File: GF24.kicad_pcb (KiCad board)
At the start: 2 copper layers, 66 parts, among them J1 3220-10-0300-00, J2 2137160001, Q1 3904, Q2 DMN3731U-7, Q3 DMN3731U-7, Q4 DMP2004K-7, Q5 DMP2004K-7, Q6 DMP2004K-7, SW1 NRST, SW2 BOOT, SW3 ACTION, SW4 ON/OFF, SW5 MODE, U1 STM32F031C4T6, U2 SAM-M10Q, U3 TPS745, U4 LTC1733, U5 M24256, Y1 CS06465-32M

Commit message: some layout changes
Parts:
- removed J2: 2137160001, MB-Conn:MOLEX_2137160001
- added U6: 2137160001, MB-Conn:MOLEX_2137160001, F.Cu at (200.0, 87.0)
- BAT1: renamed from BAT+1; moved to B.Cu
- BAT2: renamed from BAT-1; moved to B.Cu
- C11, C12, C13, Q2, Q3, Q4, Q5, Q6, R10, R15, R16, R17, R18, R19, R20, R21, R22, R23, R5, R6, R7, R8, R9, TH1, U4: moved to B.Cu
- moved BAT1 120.3 mm to (169.8, 100.0), turned to 90 degrees
- moved U5 119.9 mm to (107.0, 151.0), turned to 90 degrees
- moved R11 106.6 mm to (103.8, 148.0)
- moved C14 106.0 mm to (103.5, 151.0), turned to -90 degrees
- moved C7 105.9 mm to (85.0, 92.0), turned to 90 degrees
- moved R12 102.9 mm to (107.0, 148.0)
- moved SW1 102.5 mm to (98.0, 130.0), turned to 90 degrees
- moved Q1 95.8 mm to (154.6, 131.1), turned to 180 degrees
- moved R1 95.6 mm to (108.8, 130.7), turned to -90 degrees
- moved C3 95.5 mm to (101.8, 141.0), turned to 90 degrees
- moved SW2 95.2 mm to (109.0, 125.8), turned to 180 degrees
- moved C1 94.2 mm to (111.8, 145.8), turned to 180 degrees
- moved C6 93.8 mm to (98.0, 141.0)
- moved C5 92.1 mm to (97.5, 136.5), turned to 180 degrees
- moved SW5 91.5 mm to (182.0, 86.8), turned to 180 degrees
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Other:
- board outline added: 125 x 40 mm

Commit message: 'test'
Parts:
- moved Q5 1.69 mm to (143.5, 60.6)

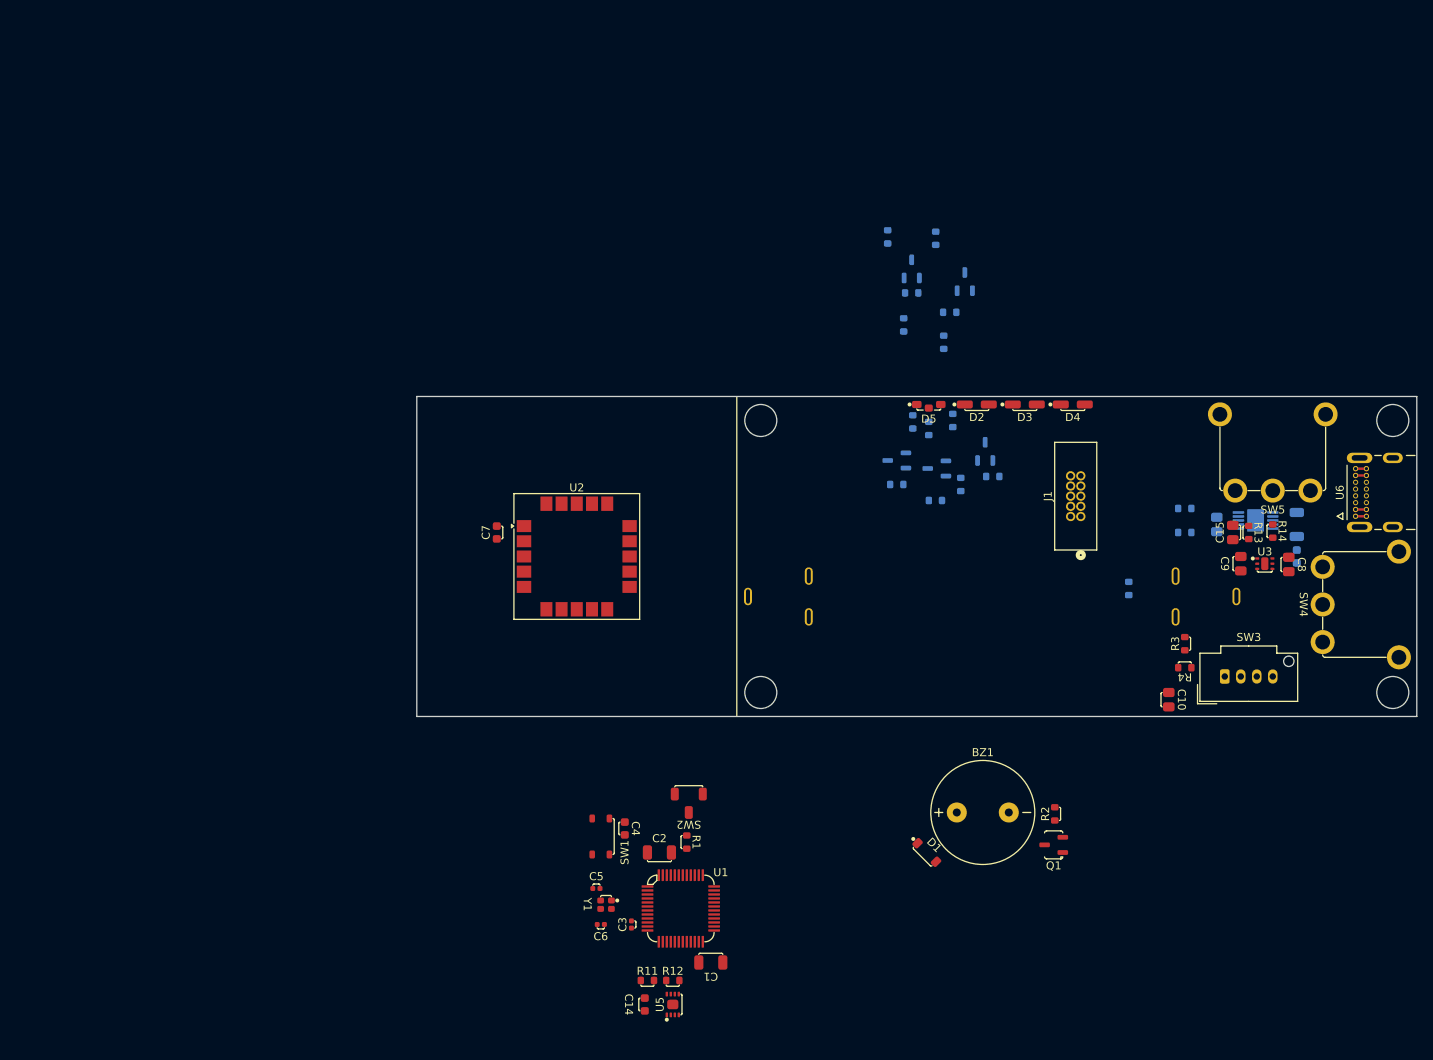
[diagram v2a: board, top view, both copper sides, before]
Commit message: started traces. need to check footprints are correct i.e. regulator
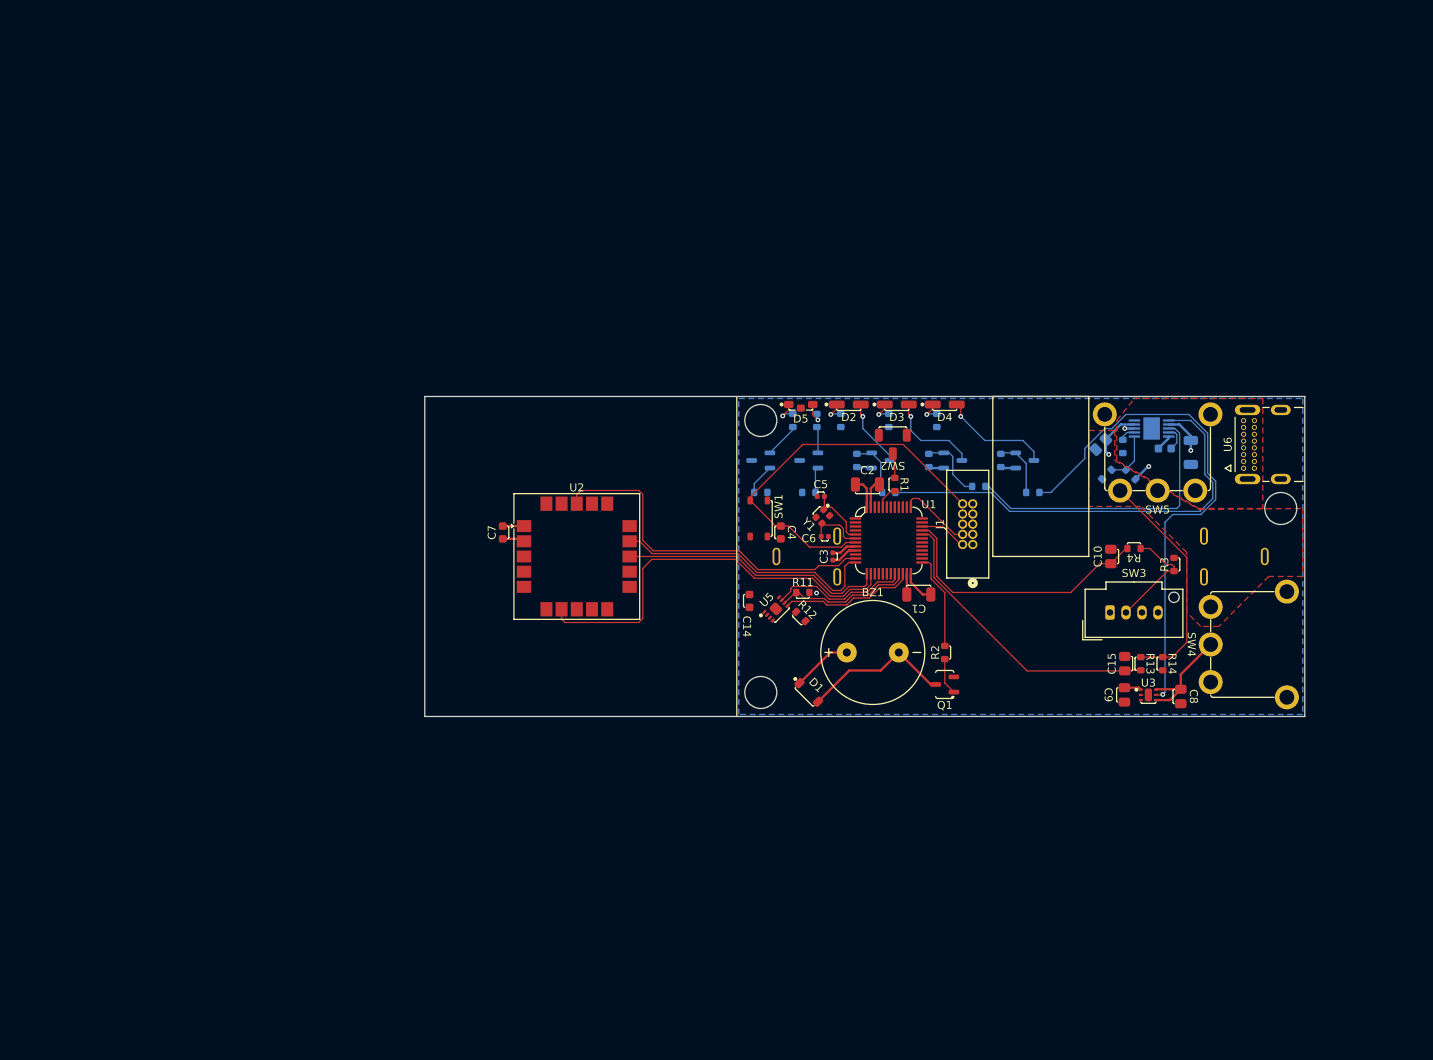
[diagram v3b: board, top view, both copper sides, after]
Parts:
- moved C5 56.5 mm to (125.5, 87.5)
- moved C6 56.0 mm to (126.0, 92.5)
- moved Y1 55.6 mm to (125.8, 90.0), turned to -135 degrees
- moved C2 52.8 mm to (131.3, 86.0)
- moved C1 52.8 mm to (137.8, 99.8)
- moved U1 52.8 mm to (134.0, 93.0)
- moved C3 52.4 mm to (127.0, 95.0)
- moved R11 52.2 mm to (123.2, 99.5)
- moved C14 52.1 mm to (116.6, 100.6)
- moved R1 51.7 mm to (134.8, 86.0)
- moved SW2 51.6 mm to (134.5, 81.0)
- moved U5 51.1 mm to (119.9, 101.6), turned to 45 degrees
- moved R12 48.2 mm to (123.0, 102.5), turned to -45 degrees
- moved SW1 44.4 mm to (117.8, 90.2)
- moved C4 41.8 mm to (120.5, 92.0)
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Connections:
- net +3V3 renamed 3V3
- net BAT- renamed GND
- net Net-(BZ1--) renamed /BUZZ-
- net Net-(D2-A) renamed /CHRG_QO
- net Net-(D2-K) renamed /CHRG_RES
- net Net-(D3-A) renamed /FAULT_QO
- net Net-(D3-K) renamed /FAULT_RES
- net Net-(D4-A) renamed /PG_QO
- net Net-(D4-K) renamed /PG_RES
- net Net-(D5-G) renamed /STATG_RES
- net Net-(D5-R) renamed /STATR_RES
- net Net-(Q1-B) renamed /BUZZ-QB
- net Net-(Q2-D) renamed /STATG_QI
- net Net-(Q2-G) renamed /STATG_QG
- net Net-(Q3-D) renamed /STATR_QI
- net Net-(Q3-G) renamed /STATR_QG
- net Net-(Q4-G) renamed /PG_QG
- net Net-(Q5-G) renamed /FAULT_QG
- net Net-(Q6-G) renamed /CHRG_QG
- net Net-(R3-Pad1) renamed /ACT-H
- net Net-(SW2-B) renamed /BOOT0_RES
- net Net-(SW4-B) renamed /REG_I
- net Net-(SW5-A) renamed /MODE-H
- net Net-(U4-NTC) renamed /CH-TH-DIV
- net Net-(U4-PROG) renamed /CH-PROG
- net Net-(U4-TIMER) renamed /CH-TIMER
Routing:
- net PG: track 0.00 -> 65.5 mm, vias 0 -> 1
- net N-CHRG: track 0.00 -> 55.0 mm
- net GNSS-TIMEPULSE: track 0.00 -> 50.9 mm
- net NRST: track 0.00 -> 48.6 mm
- net GNSS-N-RESET: track 0.00 -> 44.2 mm
- net MODE: track 0.00 -> 37.2 mm
- net N-FAULT: track 0.00 -> 36.2 mm
- net BUTTON: track 0.00 -> 33.9 mm
- net STM32-TX: track 0.00 -> 33.7 mm
- net STM32-RX: track 0.00 -> 33.4 mm
- net /MODE-H: track 0.00 -> 28.9 mm
- net 3V3: track 0.00 -> 25.8 mm
- net /BUZZ-: track 0.00 -> 18.9 mm
- net EEPROM-N-WC: track 0.00 -> 17.4 mm
- net SCL: track 0.00 -> 17.2 mm
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- added copper zone on F.Cu, net BAT+
- added copper zone on B.Cu, net GND
- added copper zone on F.Cu, net VBUS
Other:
- board size 125 x 40 mm -> 110 x 40 mm

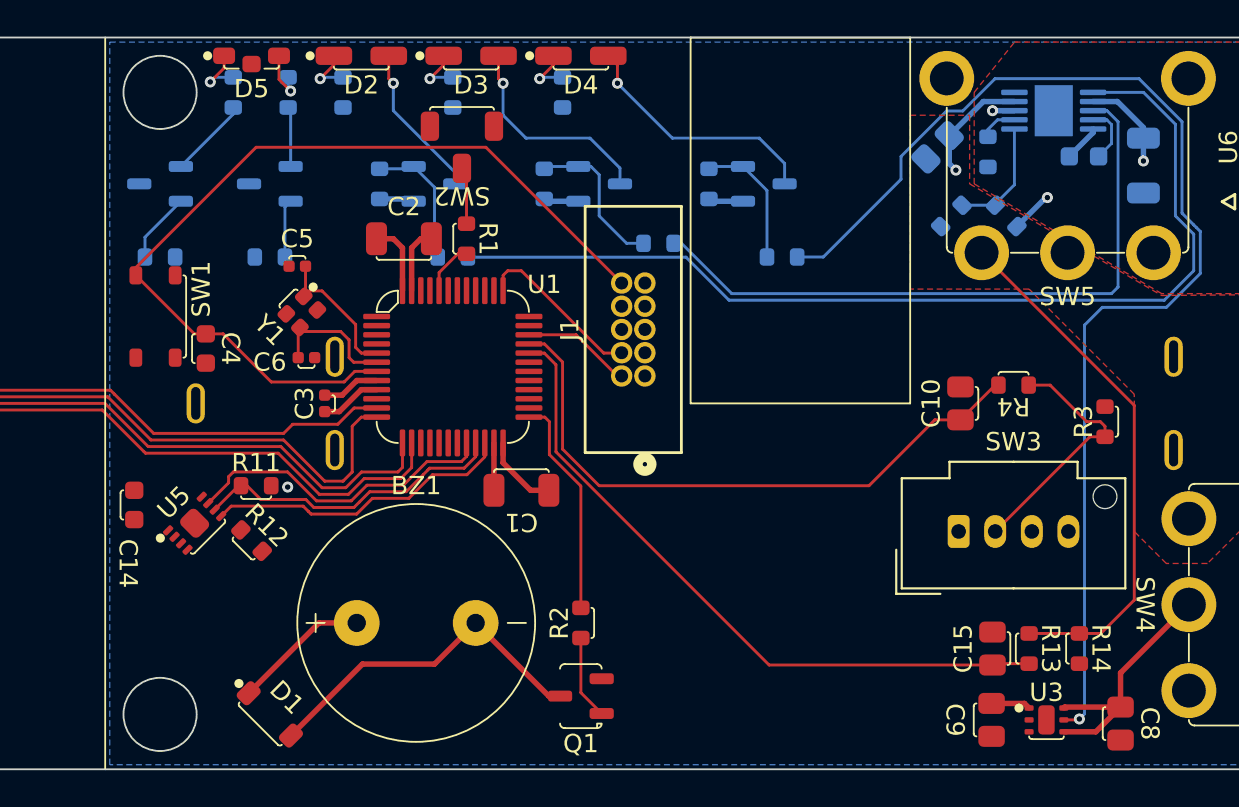
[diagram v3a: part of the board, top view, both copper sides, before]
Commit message: drew 3v plane
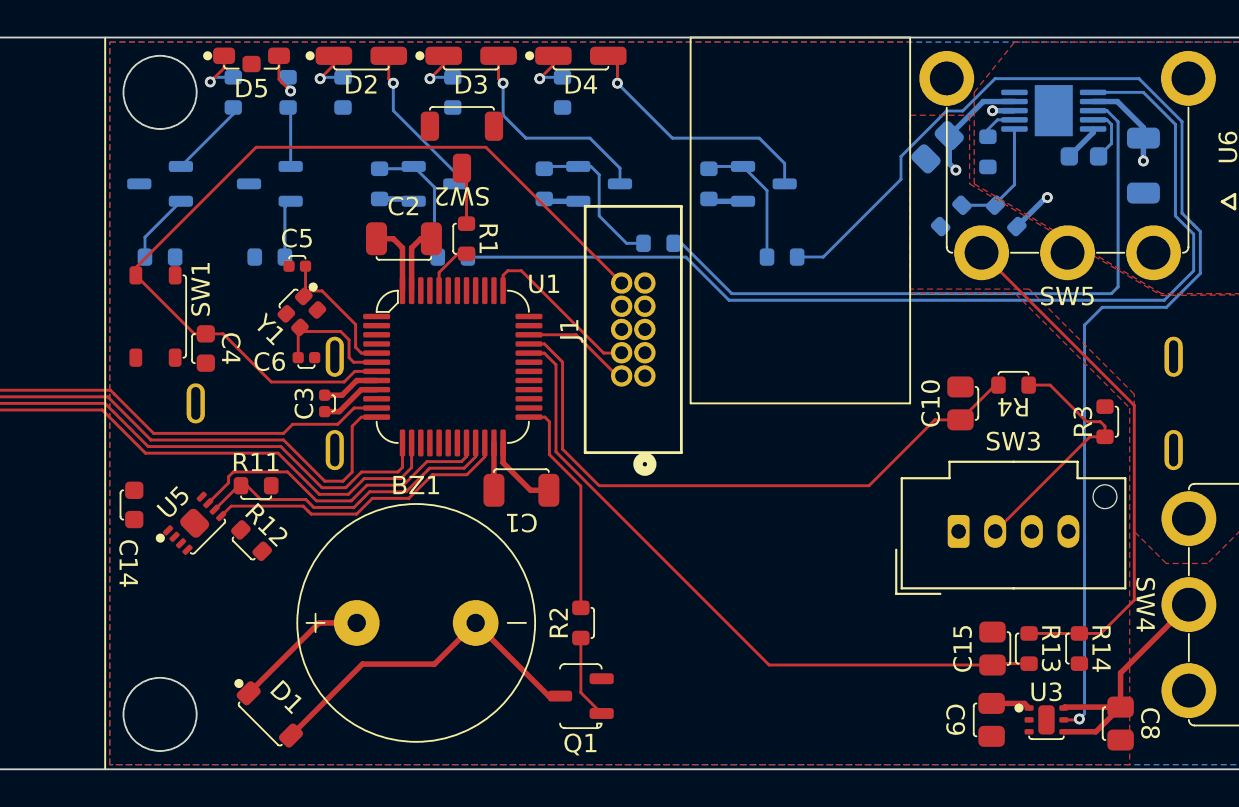
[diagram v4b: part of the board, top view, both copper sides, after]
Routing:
- net (no net): vias 1 -> 0
- added copper zone on F.Cu, net 3V3

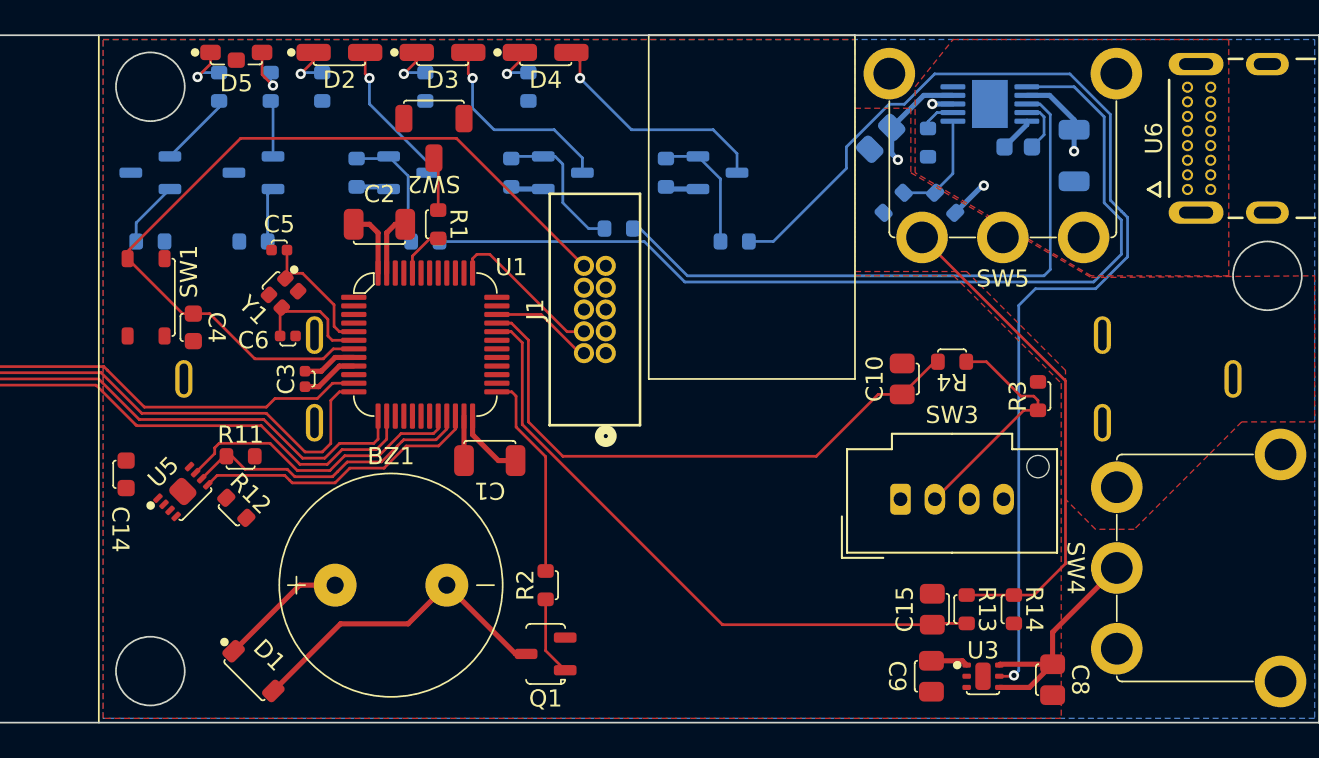
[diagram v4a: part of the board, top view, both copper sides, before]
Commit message: fixed broken footprint
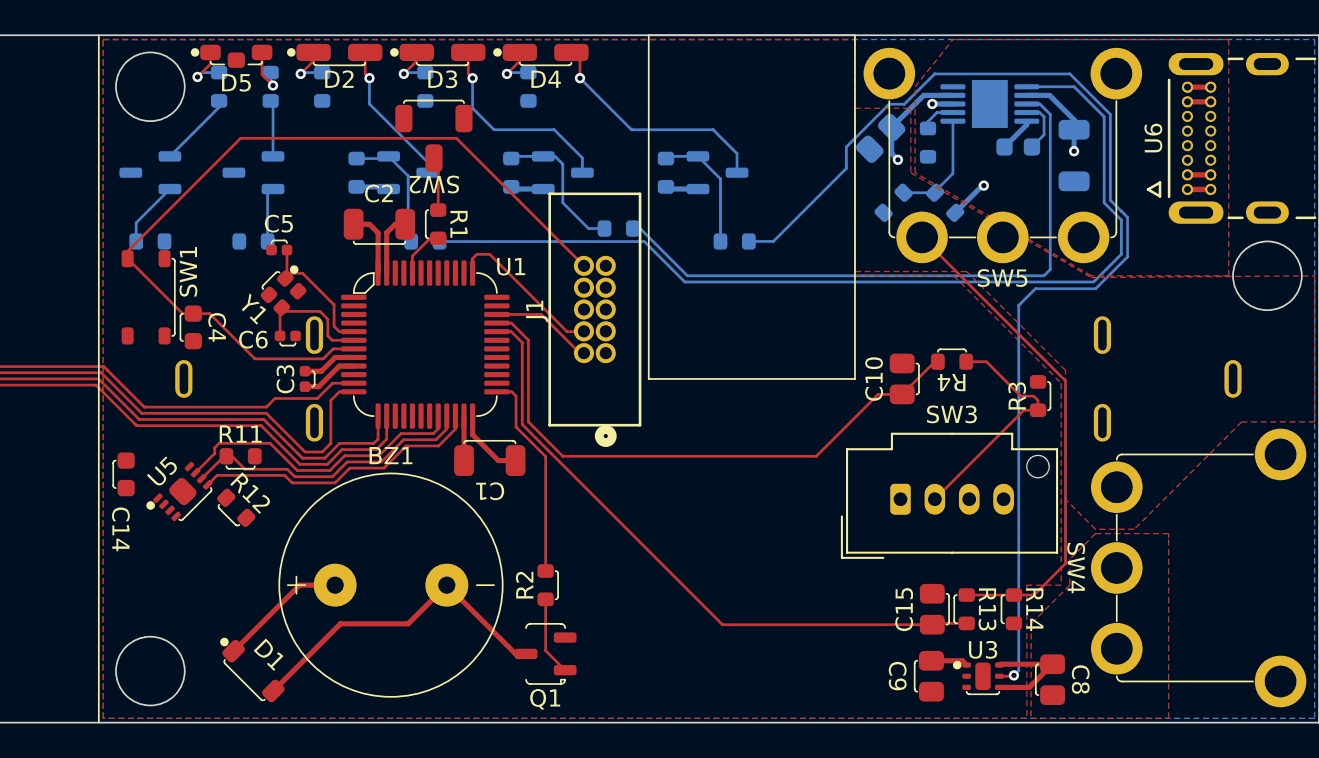
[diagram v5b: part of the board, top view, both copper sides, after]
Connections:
- U1 pad 45: unconnected-(U1-PB8-Pad45) -> STATR
- U1 pad 46: unconnected-(U1-PB9-Pad46) -> STATG
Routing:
- net /REG_I: track 13.9 -> 6.78 mm
- added copper zone on F.Cu, net /REG_I
